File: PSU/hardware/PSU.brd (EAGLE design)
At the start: 143.5 x 58.5 mm, 202 parts, among them J1 SWD, J2 UART, Q1 PMOS-DPAK, Q10 PMOS-SOT23, Q11 NPN, Q2 PMOS-SOT23, Q3 NPN, Q4 PMOS-SOT23, Q5 NMOS-SOT23, Q6 PMOS-DPAK, Q7 PMOS-SOT23, Q8 NMOS-SOT23, Q9 PMOS-DPAK, U1 LM2576, U10 4069, U11 LTV-247, U12 74HC08, U13 STM8S003K3T6C, U14 74HC08, U15 4051, U16 358, U17 358, U18 74HC32, U2 MT3608, U3 7805, U4 324, U5 MC34063, U6 MT3608, U7 LM2576, U8 MC34063, U9 TP4056

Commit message: [HW/PSU] Fix MT3608 feedback divider values
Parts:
- R15: value 10k -> 33k
- R18: value 3.3k -> 4.7k
- R4: value 33k -> 4.7k
- R5: value 3.9k -> 240
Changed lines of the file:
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@@
 <attribute name="NAME" x="110.49" y="11.43" size="1" layer="25" font="vector" ratio="10" align="bottom-center"/>
 </element>
-<element name="R4" library="rcl" library_urn="urn:adsk.eagle:library:334" package="R0805" package3d_urn="urn:adsk.eagle:package:23553/2" value="33k" x="133.35" y="48.26" smashed="yes" rot="MR180">
+<element name="R4" library="rcl" library_urn="urn:adsk.eagle:library:334" package="R0805" package3d_urn="urn:adsk.eagle:package:23553/2" value="4.7k" x="133.35" y="48.26" smashed="yes" rot="MR180">
 <attribute name="NAME" x="133.35" y="47.117" size="0.8128" layer="26" font="vector" ratio="10" rot="MR180" align="bottom-center"/>
 <attribute name="POPULARITY" value="86" x="133.35" y="48.26" size="0.254" layer="156" font="vector" ratio="10" rot="MR180" display="off"/>
@@
 <attribute name="SPICEPREFIX" value="C" x="138.43" y="41.275" size="0.254" layer="156" font="vector" ratio="10" rot="MR180" display="off"/>
 </element>
-<element name="R5" library="rcl" library_urn="urn:adsk.eagle:library:334" package="R0805" package3d_urn="urn:adsk.eagle:package:23553/2" value="3.9k" x="133.35" y="50.8" smashed="yes" rot="MR0">
+<element name="R5" library="rcl" library_urn="urn:adsk.eagle:library:334" package="R0805" package3d_urn="urn:adsk.eagle:package:23553/2" value="240" x="133.35" y="50.8" smashed="yes" rot="MR0">
 <attribute name="NAME" x="133.35" y="51.943" size="0.8128" layer="26" font="vector" ratio="10" rot="MR0" align="bottom-center"/>
 <attribute name="POPULARITY" value="86" x="133.35" y="50.8" size="0.254" layer="156" font="vector" ratio="10" rot="MR0" display="off"/>
@@
 <attribute name="NAME" x="46.355" y="49.53" size="1" layer="26" font="vector" ratio="10" rot="MR0" align="bottom-center"/>
 </element>
-<element name="R15" library="rcl" library_urn="urn:adsk.eagle:library:334" package="R0805" package3d_urn="urn:adsk.eagle:package:23553/2" value="10k" x="51.435" y="44.45" smashed="yes" rot="MR180">
+<element name="R15" library="rcl" library_urn="urn:adsk.eagle:library:334" package="R0805" package3d_urn="urn:adsk.eagle:package:23553/2" value="33k" x="51.435" y="44.45" smashed="yes" rot="MR180">
 <attribute name="NAME" x="53.594" y="44.45" size="0.8128" layer="26" font="vector" ratio="10" rot="MR180" align="center-left"/>
 <attribute name="POPULARITY" value="86" x="46.355" y="19.05" size="0.254" layer="156" font="vector" ratio="10" rot="MR180" display="off"/>
@@
 <attribute name="SPICEPREFIX" value="C" x="53.34" y="61.595" size="0.254" layer="156" font="vector" ratio="10" rot="MR270" display="off"/>
 </element>
-<element name="R18" library="rcl" library_urn="urn:adsk.eagle:library:334" package="R0805" package3d_urn="urn:adsk.eagle:package:23553/2" value="3.3k" x="46.99" y="44.45" smashed="yes" rot="MR180">
+<element name="R18" library="rcl" library_urn="urn:adsk.eagle:library:334" package="R0805" package3d_urn="urn:adsk.eagle:package:23553/2" value="4.7k" x="46.99" y="44.45" smashed="yes" rot="MR180">
 <attribute name="NAME" x="44.831" y="44.45" size="0.8128" layer="26" font="vector" ratio="10" rot="MR0" align="center-left"/>
 <attribute name="POPULARITY" value="86" x="15.24" y="46.99" size="0.254" layer="156" font="vector" ratio="10" rot="MR180" display="off"/>

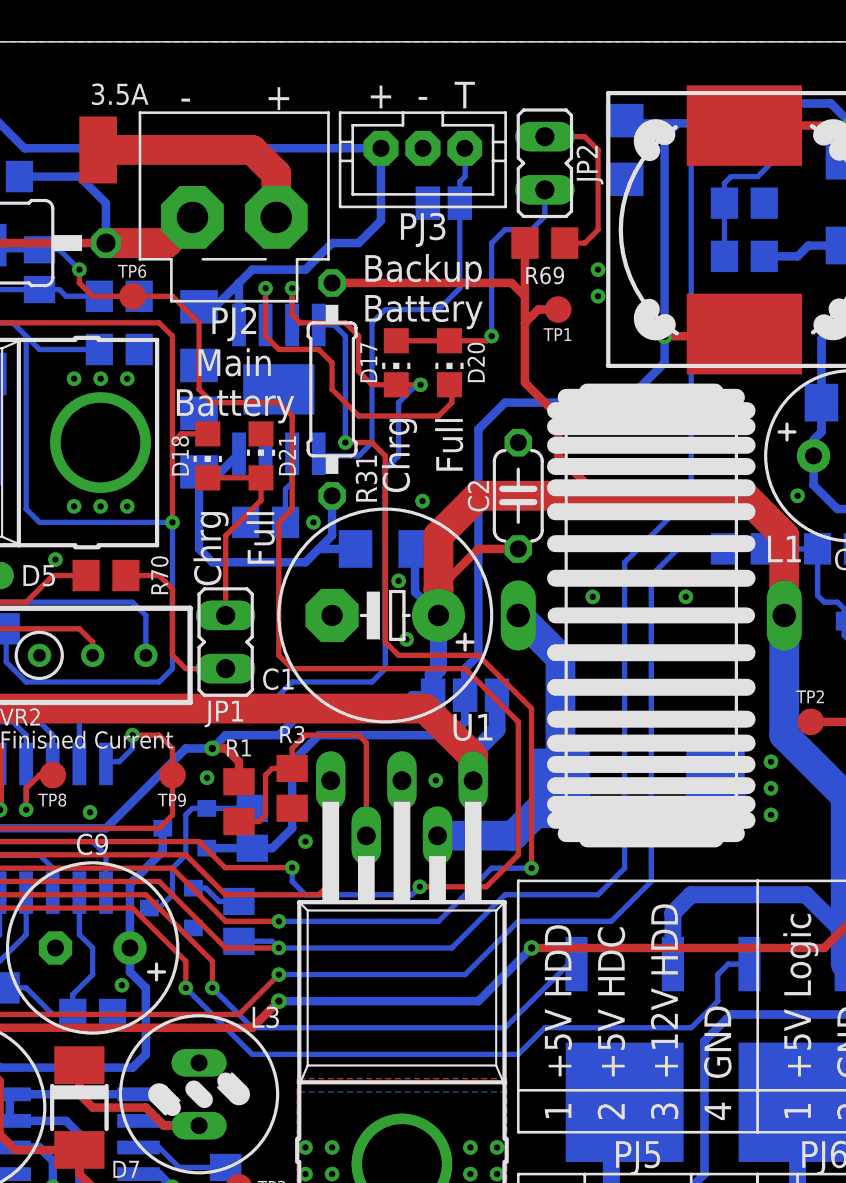
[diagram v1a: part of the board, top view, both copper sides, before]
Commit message: [HW/PSU] Fix secondary 12V regulator enabling
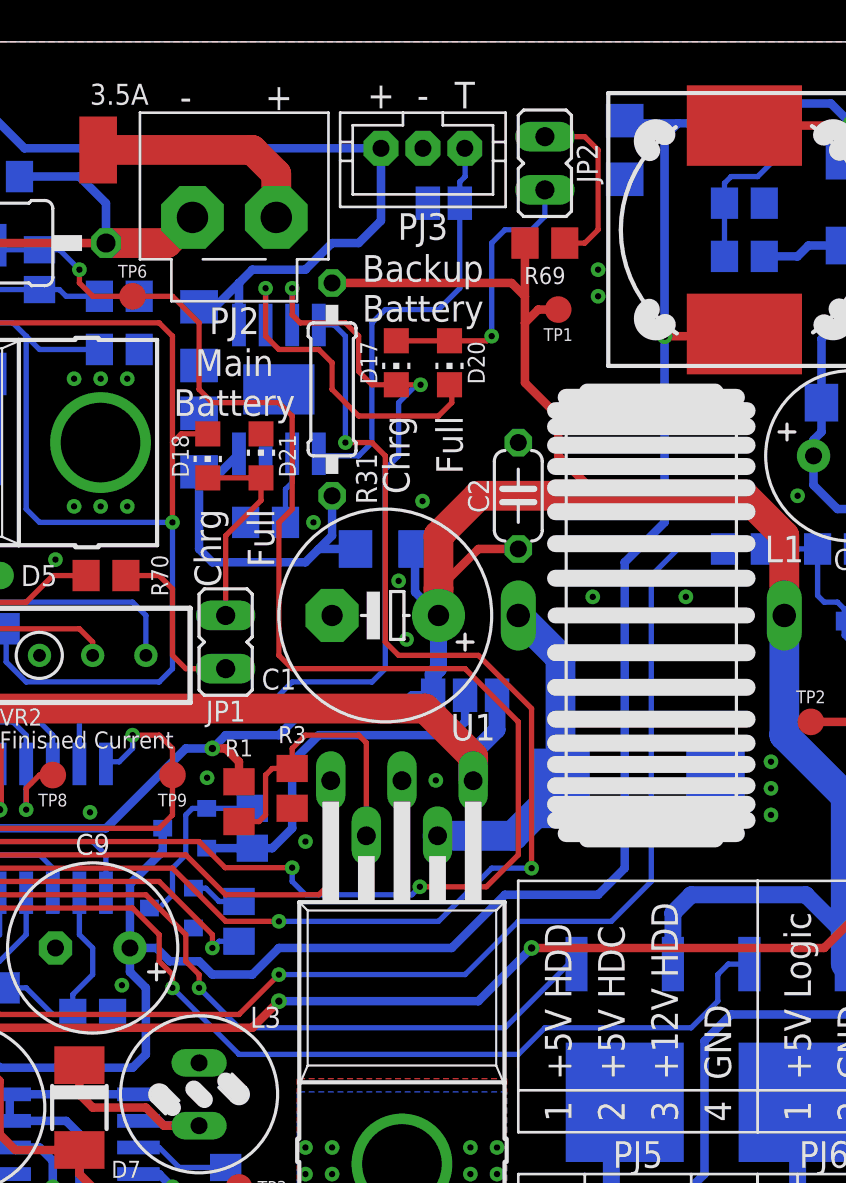
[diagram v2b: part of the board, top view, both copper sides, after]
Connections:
- net SEC_CTRL: no longer U2.4
- net SEC_VIN: no longer C4.1, L2.1, U2.5
- net SEC_VIN_SW: now also C4.1, L2.1, U2.4, U2.5
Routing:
- net SEC_VIN_SW: track 66.9 -> 139.0 mm, vias 3 -> 4
- net SEC_CTRL: track 150.7 -> 92.3 mm
- net SEC_VIN: track 61.1 -> 18.0 mm, vias 1 -> 0
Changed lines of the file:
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@@
 <signal name="SEC_VIN" class="2">
 <contactref element="SJ2" pad="2"/>
-<contactref element="U2" pad="5"/>
-<contactref element="C4" pad="1"/>
 <contactref element="Q2" pad="2"/>
 <contactref element="R6" pad="2"/>
-<contactref element="L2" pad="1"/>
-<via x="129.54" y="44.45" extent="1-16" drill="0.35" shape="octagon"/>
-<wire x1="131.9749" y1="54.61" x2="130.175" y2="54.61" width="0.4064" layer="16"/>
-<wire x1="130.175" y1="54.61" x2="127.765" y2="54.61" width="0.4064" layer="16"/>
-<wire x1="127.765" y1="54.61" x2="127.635" y2="54.74" width="0.4064" layer="16"/>
-<wire x1="129.54" y1="53.975" x2="130.175" y2="54.61" width="0.4064" layer="16"/>
-<wire x1="129.54" y1="53.975" x2="129.54" y2="44.45" width="0.4064" layer="16"/>
-<wire x1="129.54" y1="44.45" x2="129.54" y2="43.18" width="0.4064" layer="16"/>
-<wire x1="129.54" y1="43.18" x2="127.635" y2="41.275" width="0.4064" layer="16"/>
-<wire x1="127.635" y1="41.275" x2="121.92" y2="41.275" width="0.4064" layer="16"/>
-<wire x1="121.92" y1="41.275" x2="120.65" y2="40.005" width="0.4064" layer="16"/>
-<wire x1="120.65" y1="40.005" x2="120.65" y2="29.21" width="0.4064" layer="16"/>
-<wire x1="120.65" y1="29.21" x2="120.015" y2="28.575" width="0.4064" layer="16"/>
-<wire x1="120.015" y1="28.575" x2="120.015" y2="27.305" width="0.4064" layer="16"/>
 <wire x1="120.015" y1="27.305" x2="120.015" y2="26.035" width="0.4064" layer="16"/>
 <wire x1="120.015" y1="26.035" x2="119.38" y2="25.4" width="0.4064" layer="16"/>
@@
 <wire x1="109.855" y1="20.005" x2="107.68" y2="20.005" width="0.4064" layer="16"/>
 <wire x1="109.855" y1="20.005" x2="110.81" y2="20.005" width="0.4064" layer="16"/>
-<wire x1="133.245" y1="44.45" x2="129.54" y2="44.45" width="0.4064" layer="1"/>
-<wire x1="133.35" y1="44.555" x2="133.245" y2="44.45" width="0.4064" layer="1"/>
 </signal>
 <signal name="SEC_CTRL" class="1">
-<contactref element="U2" pad="4"/>
 <contactref element="R7" pad="1"/>
-<wire x1="131.9749" y1="53.66" x2="131.13" y2="53.66" width="0.254" layer="16"/>
-<wire x1="131.13" y1="53.66" x2="130.81" y2="53.34" width="0.254" layer="16"/>
-<wire x1="130.81" y1="36.83" x2="127.635" y2="33.655" width="0.254" layer="16"/>
-<wire x1="130.81" y1="53.34" x2="130.81" y2="36.83" width="0.254" layer="16"/>
-<wire x1="127.635" y1="33.655" x2="127.635" y2="19.05" width="0.254" layer="16"/>
-<wire x1="127.635" y1="19.05" x2="126.365" y2="17.78" width="0.254" layer="16"/>
-<wire x1="126.365" y1="17.78" x2="121.92" y2="17.78" width="0.254" layer="16"/>
-<wire x1="121.92" y1="17.78" x2="119.38" y2="15.24" width="0.254" layer="16"/>
-<wire x1="119.38" y1="15.24" x2="111.125" y2="15.24" width="0.254" layer="16"/>
-<via x="111.125" y="15.24" extent="1-16" drill="0.3" shape="octagon"/>
-<wire x1="111.125" y1="15.24" x2="108.585" y2="15.24" width="0.254" layer="1"/>
-<wire x1="108.585" y1="15.24" x2="105.41" y2="18.415" width="0.254" layer="1"/>
+<via x="107.95" y="15.24" extent="1-16" drill="0.3" shape="octagon"/>
+<wire x1="107.95" y1="15.24" x2="107.95" y2="15.875" width="0.254" layer="1"/>
+<wire x1="107.95" y1="15.875" x2="105.41" y2="18.415" width="0.254" layer="1"/>
 <wire x1="105.41" y1="18.415" x2="94.615" y2="18.415" width="0.254" layer="1"/>
 <wire x1="94.615" y1="18.415" x2="93.98" y2="19.05" width="0.254" layer="1"/>
@@
 <wire x1="46.355" y1="38.1" x2="46.99" y2="38.1" width="0.254" layer="1"/>
 <wire x1="46.99" y1="38.1" x2="48.26" y2="36.83" width="0.254" layer="1"/>
-<wire x1="109.22" y1="15.56" x2="110.805" y2="15.56" width="0.254" layer="16"/>
-<wire x1="110.805" y1="15.56" x2="111.125" y2="15.24" width="0.254" layer="16"/>
+<wire x1="109.22" y1="15.56" x2="108.27" y2="15.56" width="0.254" layer="16"/>
+<wire x1="108.27" y1="15.56" x2="107.95" y2="15.24" width="0.254" layer="16"/>
 </signal>
 <signal name="SECV_G" class="1">
@@
 <via x="91.44" y="3.175" extent="1-16" drill="0.35" shape="octagon"/>
 <wire x1="91.44" y1="3.175" x2="91.44" y2="9.525" width="0.4064" layer="16"/>
+<contactref element="U2" pad="5"/>
+<contactref element="C4" pad="1"/>
+<contactref element="L2" pad="1"/>
+<contactref element="U2" pad="4"/>
+<via x="129.54" y="44.45" extent="1-16" drill="0.35" shape="octagon"/>
+<wire x1="131.9749" y1="54.61" x2="130.175" y2="54.61" width="0.4064" layer="16"/>
+<wire x1="127.765" y1="54.61" x2="130.175" y2="54.61" width="0.4064" layer="16"/>
+<wire x1="127.765" y1="54.61" x2="127.635" y2="54.74" width="0.4064" layer="16"/>
+<wire x1="129.54" y1="53.975" x2="130.175" y2="54.61" width="0.4064" layer="16"/>
+<wire x1="129.54" y1="53.975" x2="129.54" y2="44.45" width="0.4064" layer="16"/>
+<wire x1="133.245" y1="44.45" x2="129.54" y2="44.45" width="0.4064" layer="1"/>
+<wire x1="133.35" y1="44.555" x2="133.245" y2="44.45" width="0.4064" layer="1"/>
+<wire x1="131.9749" y1="53.66" x2="131.9749" y2="54.61" width="0.4064" layer="16"/>
+<wire x1="129.54" y1="35.56" x2="127.635" y2="33.655" width="0.4064" layer="16"/>
+<wire x1="127.635" y1="19.05" x2="126.365" y2="17.78" width="0.4064" layer="16"/>
+<wire x1="126.365" y1="17.78" x2="121.92" y2="17.78" width="0.4064" layer="16"/>
+<wire x1="121.92" y1="17.78" x2="119.38" y2="15.24" width="0.4064" layer="16"/>
+<wire x1="127.635" y1="33.655" x2="127.635" y2="19.05" width="0.4064" layer="16"/>
+<wire x1="129.54" y1="44.45" x2="129.54" y2="35.56" width="0.4064" layer="16"/>
+<wire x1="119.38" y1="15.24" x2="111.125" y2="15.24" width="0.4064" layer="16"/>
+<wire x1="111.125" y1="15.24" x2="109.855" y2="13.97" width="0.4064" layer="16"/>
+<wire x1="109.855" y1="13.97" x2="107.95" y2="13.97" width="0.4064" layer="16"/>
+<wire x1="107.95" y1="13.97" x2="107.315" y2="14.605" width="0.4064" layer="16"/>
+<wire x1="105.918" y1="14.605" x2="105.283" y2="15.24" width="0.4064" layer="16"/>
+<wire x1="105.283" y1="15.24" x2="104.013" y2="15.24" width="0.4064" layer="16"/>
+<wire x1="107.315" y1="14.605" x2="105.918" y2="14.605" width="0.4064" layer="16"/>
 </signal>
 <signal name="-22V_SWC" class="2">
@@
 <wire x1="122.555" y1="10.16" x2="123.825" y2="11.43" width="0.254" layer="16"/>
 <wire x1="130.81" y1="11.43" x2="123.825" y2="11.43" width="0.254" layer="16"/>
-<wire x1="122.555" y1="10.16" x2="109.855" y2="10.16" width="0.254" layer="16"/>
-<via x="106.68" y="13.335" extent="1-16" drill="0.3" shape="octagon"/>
-<wire x1="106.68" y1="13.335" x2="106.68" y2="14.605" width="0.254" layer="1"/>
-<wire x1="106.68" y1="14.605" x2="104.14" y2="17.145" width="0.254" layer="1"/>
+<wire x1="122.555" y1="10.16" x2="109.22" y2="10.16" width="0.254" layer="16"/>
+<via x="106.045" y="13.335" extent="1-16" drill="0.3" shape="octagon"/>
+<wire x1="105.41" y1="15.875" x2="105.41" y2="14.605" width="0.254" layer="1"/>
+<wire x1="106.045" y1="13.335" x2="106.045" y2="13.97" width="0.254" layer="1"/>
+<wire x1="106.045" y1="13.97" x2="105.41" y2="14.605" width="0.254" layer="1"/>
+<wire x1="105.41" y1="15.875" x2="104.14" y2="17.145" width="0.254" layer="1"/>
 <wire x1="104.14" y1="17.145" x2="92.075" y2="17.145" width="0.254" layer="1"/>
 <wire x1="90.805" y1="18.415" x2="77.47" y2="18.415" width="0.254" layer="1"/>
@@
 <contactref element="U10" pad="2"/>
 <wire x1="76.835" y1="19.05" x2="76.835" y2="20.4216" width="0.254" layer="1"/>
-<wire x1="106.68" y1="13.335" x2="109.855" y2="10.16" width="0.254" layer="16"/>
+<wire x1="106.045" y1="13.335" x2="109.22" y2="10.16" width="0.254" layer="16"/>
 </signal>
 <signal name="+5VHDD_G" class="1">
 <contactref element="Q9" pad="1"/>
-<via x="107.95" y="13.335" extent="1-16" drill="0.3" shape="octagon"/>
-<wire x1="107.95" y1="13.335" x2="107.95" y2="14.605" width="0.254" layer="1"/>
-<wire x1="107.95" y1="14.605" x2="104.775" y2="17.78" width="0.254" layer="1"/>
+<via x="107.315" y="13.335" extent="1-16" drill="0.3" shape="octagon"/>
+<wire x1="106.68" y1="15.875" x2="106.68" y2="14.605" width="0.254" layer="1"/>
+<wire x1="107.315" y1="13.335" x2="107.315" y2="13.97" width="0.254" layer="1"/>
+<wire x1="107.315" y1="13.97" x2="106.68" y2="14.605" width="0.254" layer="1"/>
+<wire x1="106.68" y1="15.875" x2="104.775" y2="17.78" width="0.254" layer="1"/>
 <wire x1="104.775" y1="17.78" x2="93.98" y2="17.78" width="0.254" layer="1"/>
 <wire x1="93.345" y1="18.415" x2="93.98" y2="17.78" width="0.254" layer="1"/>
 <wire x1="124.96" y1="14.47" x2="125.335" y2="14.47" width="0.254" layer="16"/>
-<wire x1="121.92" y1="11.43" x2="109.855" y2="11.43" width="0.254" layer="16"/>
+<wire x1="121.92" y1="11.43" x2="109.22" y2="11.43" width="0.254" layer="16"/>
 <wire x1="121.92" y1="11.43" x2="124.96" y2="14.47" width="0.254" layer="16"/>
-<wire x1="109.855" y1="11.43" x2="107.95" y2="13.335" width="0.254" layer="16"/>
+<wire x1="109.22" y1="11.43" x2="107.315" y2="13.335" width="0.254" layer="16"/>
 <wire x1="83.82" y1="22.225" x2="84.455" y2="21.59" width="0.254" layer="1"/>
 <wire x1="83.82" y1="22.225" x2="80.01" y2="22.225" width="0.254" layer="1"/>

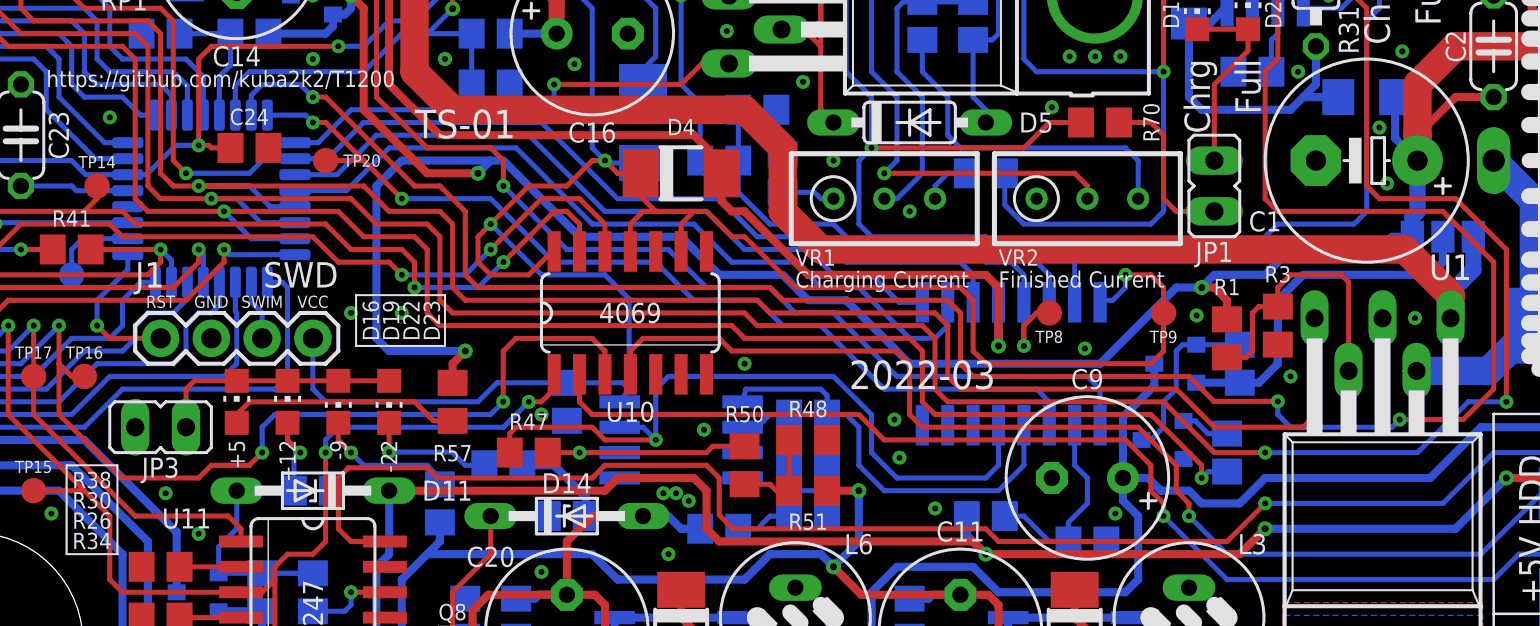
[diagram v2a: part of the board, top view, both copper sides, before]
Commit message: [HW/PSU] Fix LM2576 enable signals level
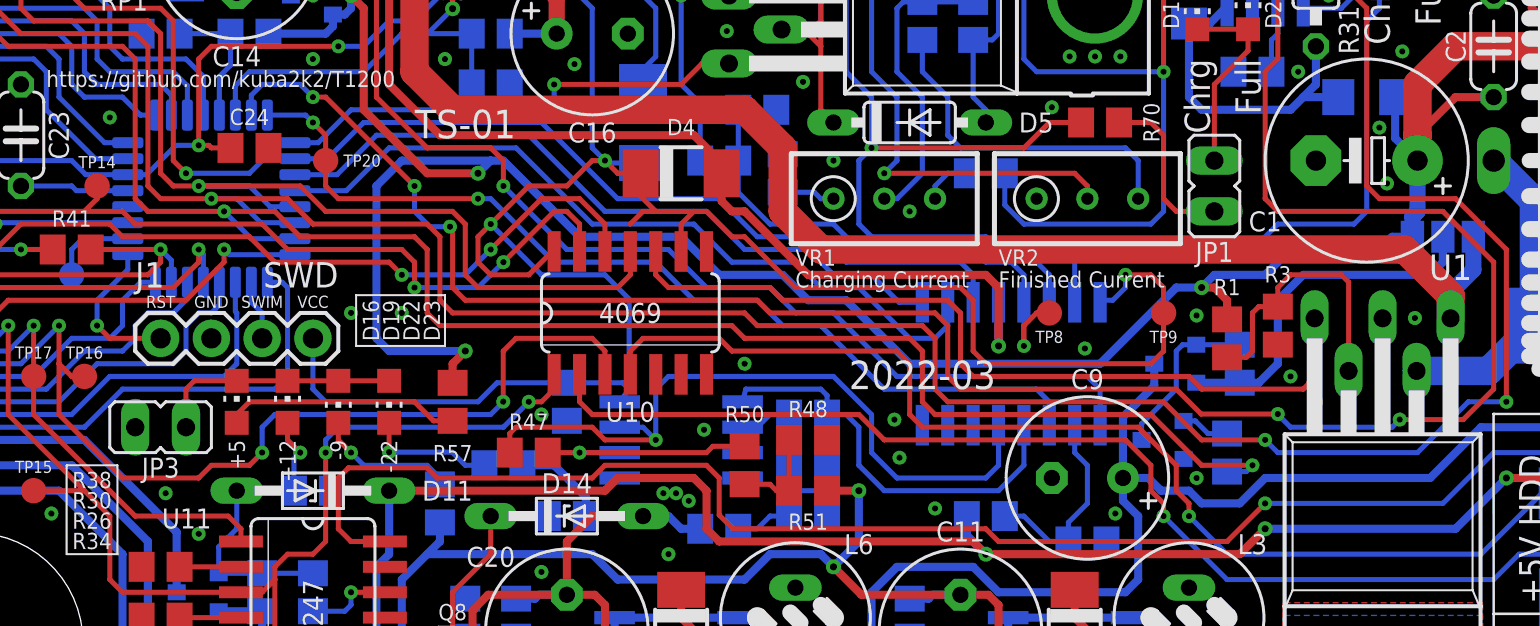
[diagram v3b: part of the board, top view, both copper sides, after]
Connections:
- net CHG_CTRL renamed ^CHG_CTRL
- new net ^PRI_CTRL: U1.5, U10.10
- net PRI_CTRL: now also U10.11; no longer U1.5
- net VCCIO: no longer U10.11
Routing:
- net PRI_CTRL: track 111.4 -> 68.7 mm
- net ^PRI_CTRL: track 0.00 -> 41.2 mm
- net SEC_CTRL: track 92.3 -> 94.2 mm
- net VCCIO: track 183.3 -> 181.9 mm
- net AIN_IBAT: track 125.3 -> 125.6 mm, vias 4 -> 6
